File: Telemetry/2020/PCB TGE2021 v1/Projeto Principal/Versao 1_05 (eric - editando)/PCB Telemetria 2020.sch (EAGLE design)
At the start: 49 parts, among them IC1 INA240A1DR, IC2 MCP3221A6T-E_OTVAO, IC3 AZ1117IH-3.3TRG1, IC4 ACS758LCB-050B-PFF-T, IC5 ADS1115IDGSR, IC6 ACS712-030B3, IC7 THVD2410DR, J1 172042-0406

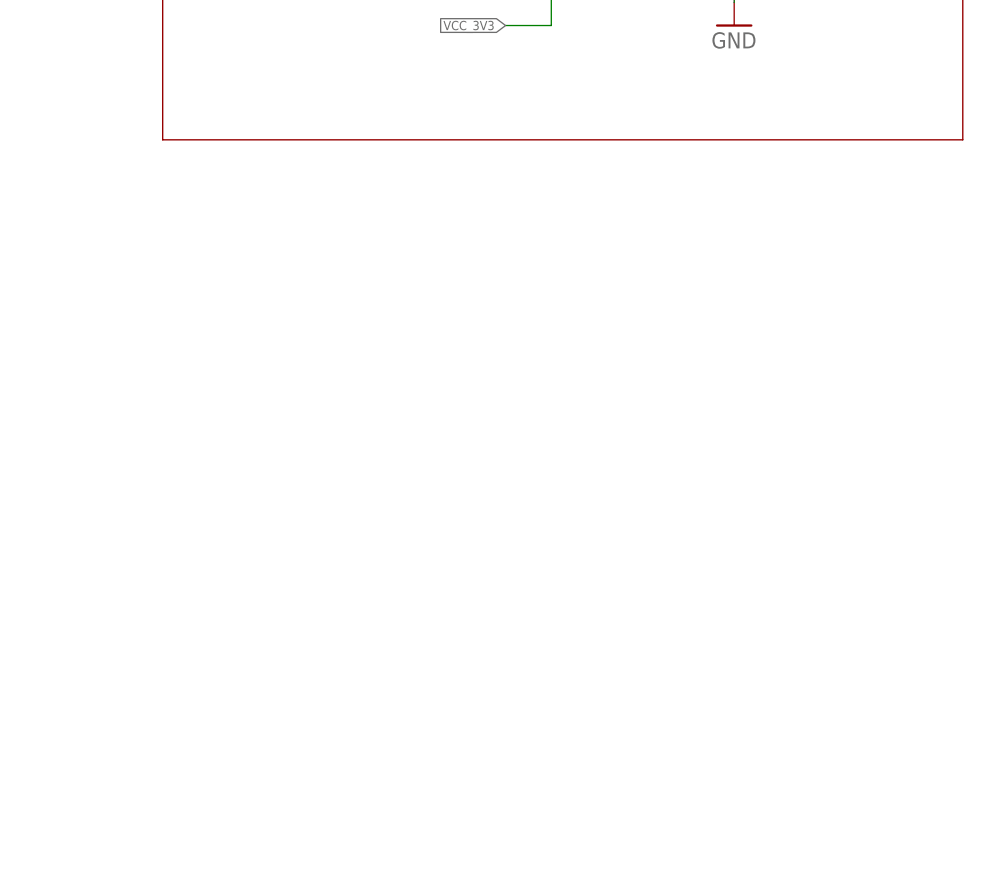
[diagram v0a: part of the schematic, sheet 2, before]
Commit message: Adding temperature sensor TMP100
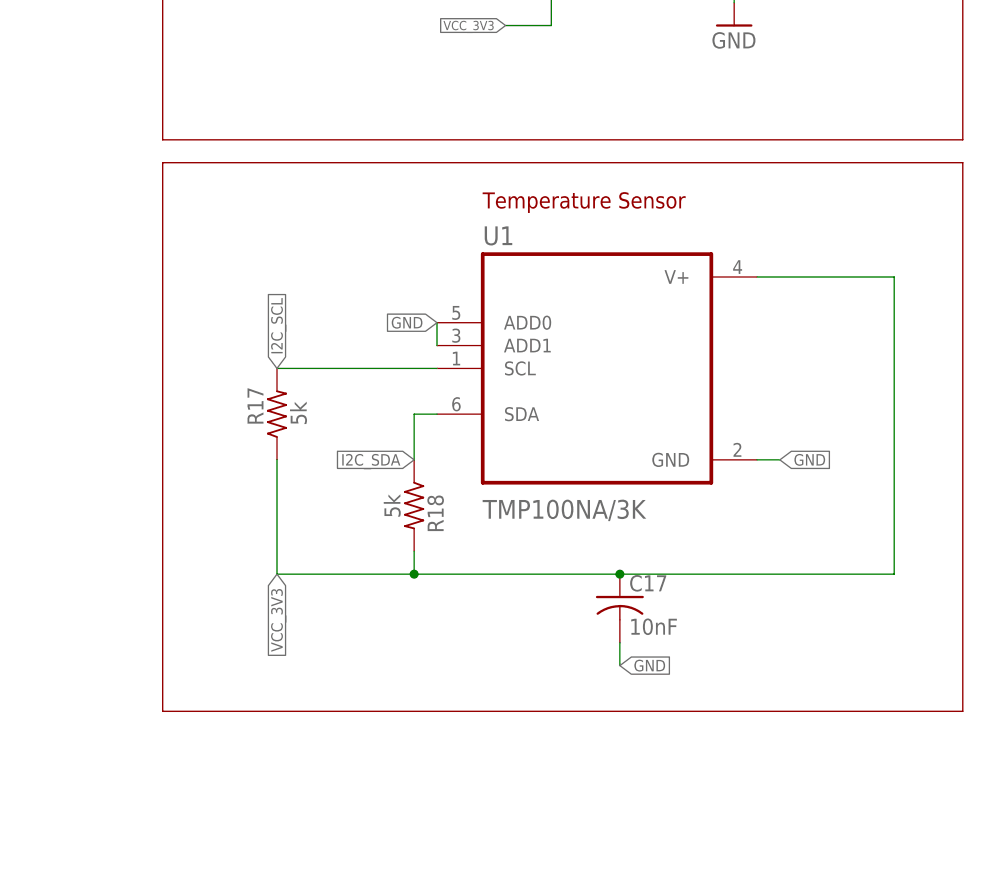
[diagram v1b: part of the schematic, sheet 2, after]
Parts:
- added C17: 10nF, rcl:C-USC0805
- added R17, R18: 5k, rcl:R-US_R0805
- added U1: TMP100NA/3K, TMP100NA_3K:TMP100NA/3K
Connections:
- net GND: now also C17.2, U1.ADD0, U1.ADD1, U1.GND
- net I2C_SCL: now also R17.2, U1.SCL
- net I2C_SDA: now also R18.1, U1.SDA
- net VCC_3V3: now also C17.1, R17.1, R18.2, U1.V+
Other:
- note added: "Temperature Sensor"
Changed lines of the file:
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@@
 <?xml version="1.0" encoding="utf-8"?>
 <!DOCTYPE eagle SYSTEM "eagle.dtd">
-<eagle version="9.5.2">
+<eagle version="9.6.2">
 <drawing>
 <settings>
@@
 <part name="SUPPLY5" library="supply2" library_urn="urn:adsk.eagle:library:372" deviceset="GND" device=""/>
 <part name="SUPPLY6" library="supply2" library_urn="urn:adsk.eagle:library:372" deviceset="GND" device=""/>
+<part name="U1" library="TMP100NA_3K" deviceset="TMP100NA/3K" device=""/>
+<part name="R17" library="rcl" library_urn="urn:adsk.eagle:library:334" deviceset="R-US_" device="R0805" package3d_urn="urn:adsk.eagle:package:23553/2" value="5k"/>
+<part name="R18" library="rcl" library_urn="urn:adsk.eagle:library:334" deviceset="R-US_" device="R0805" package3d_urn="urn:adsk.eagle:package:23553/2" value="5k"/>
+<part name="C17" library="rcl" library_urn="urn:adsk.eagle:library:334" deviceset="C-US" device="C0805" package3d_urn="urn:adsk.eagle:package:23617/2" value="10nF"/>
 </parts>
 <sheets>
@@
 <text x="365.76" y="194.564" size="1.778" layer="97" align="center">Output RC
 Filter</text>
+<wire x1="284.48" y1="142.24" x2="284.48" y2="81.28" width="0.1524" layer="94"/>
+<wire x1="284.48" y1="142.24" x2="373.38" y2="142.24" width="0.1524" layer="94"/>
+<wire x1="373.38" y1="81.28" x2="373.38" y2="142.24" width="0.1524" layer="94"/>
+<wire x1="284.48" y1="81.28" x2="373.38" y2="81.28" width="0.1524" layer="94"/>
+<text x="320.04" y="137.16" size="1.778" layer="94">Temperature Sensor</text>
 </plain>
 <instances>
@@
 <attribute name="NAME" x="326.1614" y="166.37" size="1.778" layer="95" rot="R90"/>
 <attribute name="VALUE" x="330.962" y="166.37" size="1.778" layer="96" rot="R90"/>
+</instance>
+<instance part="U1" gate="A" x="332.74" y="119.38" smashed="yes">
+<attribute name="NAME" x="320.04" y="133.08" size="2.0828" layer="95" ratio="10" rot="SR0"/>
+<attribute name="VALUE" x="320.04" y="102.68" size="2.0828" layer="96" ratio="10" rot="SR0"/>
+</instance>
+<instance part="R17" gate="G$1" x="297.18" y="114.3" smashed="yes" rot="R90">
+<attribute name="NAME" x="295.6814" y="113.03" size="1.778" layer="95" rot="R90"/>
+<attribute name="VALUE" x="300.482" y="113.03" size="1.778" layer="96" rot="R90"/>
+</instance>
+<instance part="R18" gate="G$1" x="312.42" y="104.14" smashed="yes" rot="R270">
+<attribute name="NAME" x="313.9186" y="105.41" size="1.778" layer="95" rot="R270"/>
+<attribute name="VALUE" x="309.118" y="105.41" size="1.778" layer="96" rot="R270"/>
+</instance>
+<instance part="C17" gate="G$1" x="335.28" y="93.98" smashed="yes">
+<attribute name="NAME" x="336.296" y="94.615" size="1.778" layer="95"/>
+<attribute name="VALUE" x="336.296" y="89.789" size="1.778" layer="96"/>
 </instance>
 </instances>
@@
 <wire x1="347.98" y1="160.02" x2="347.98" y2="162.56" width="0.1524" layer="91"/>
 </segment>
+<segment>
+<pinref part="U1" gate="A" pin="ADD0"/>
+<pinref part="U1" gate="A" pin="ADD1"/>
+<wire x1="314.96" y1="124.46" x2="314.96" y2="121.92" width="0.1524" layer="91"/>
+<label x="314.96" y="124.46" size="1.27" layer="95" rot="R180" xref="yes"/>
+</segment>
+<segment>
+<pinref part="U1" gate="A" pin="GND"/>
+<wire x1="350.52" y1="109.22" x2="353.06" y2="109.22" width="0.1524" layer="91"/>
+<label x="353.06" y="109.22" size="1.27" layer="95" xref="yes"/>
+</segment>
+<segment>
+<pinref part="C17" gate="G$1" pin="2"/>
+<wire x1="335.28" y1="88.9" x2="335.28" y2="86.36" width="0.1524" layer="91"/>
+<label x="335.28" y="86.36" size="1.27" layer="95" xref="yes"/>
+</segment>
 </net>
 <net name="VCC_3V3" class="0">
@@
 <wire x1="327.66" y1="157.48" x2="322.58" y2="157.48" width="0.1524" layer="91"/>
 </segment>
+<segment>
+<pinref part="R18" gate="G$1" pin="2"/>
+<pinref part="C17" gate="G$1" pin="1"/>
+<wire x1="312.42" y1="99.06" x2="312.42" y2="96.52" width="0.1524" layer="91"/>
+<wire x1="312.42" y1="96.52" x2="335.28" y2="96.52" width="0.1524" layer="91"/>
+<pinref part="R17" gate="G$1" pin="1"/>
+<wire x1="297.18" y1="109.22" x2="297.18" y2="96.52" width="0.1524" layer="91"/>
+<wire x1="297.18" y1="96.52" x2="312.42" y2="96.52" width="0.1524" layer="91"/>
+<junction x="312.42" y="96.52"/>
+<pinref part="U1" gate="A" pin="V+"/>
+<wire x1="350.52" y1="129.54" x2="365.76" y2="129.54" width="0.1524" layer="91"/>
+<wire x1="365.76" y1="129.54" x2="365.76" y2="96.52" width="0.1524" layer="91"/>
+<wire x1="365.76" y1="96.52" x2="335.28" y2="96.52" width="0.1524" layer="91"/>
+<junction x="335.28" y="96.52"/>
+<label x="297.18" y="96.52" size="1.27" layer="95" rot="R270" xref="yes"/>
+</segment>
 </net>
 <net name="MSHUNT_AMP" class="0">
@@
 <label x="76.2" y="200.66" size="1.27" layer="95" rot="R90" xref="yes"/>
 </segment>
+<segment>
+<pinref part="R18" gate="G$1" pin="1"/>
+<pinref part="U1" gate="A" pin="SDA"/>
+<wire x1="312.42" y1="109.22" x2="312.42" y2="114.3" width="0.1524" layer="91"/>
+<wire x1="312.42" y1="114.3" x2="314.96" y2="114.3" width="0.1524" layer="91"/>
+<label x="312.42" y="109.22" size="1.27" layer="95" rot="R180" xref="yes"/>
+</segment>
 </net>
 <net name="I2C_SCL" class="0">
@@
 <label x="73.66" y="200.66" size="1.27" layer="95" rot="R90" xref="yes"/>
 </segment>
-</net>
+<segment>
+<pinref part="R17" gate="G$1" pin="2"/>
+<pinref part="U1" gate="A" pin="SCL"/>
+<wire x1="297.18" y1="119.38" x2="314.96" y2="119.38" width="0.1524" layer="91"/>
+<label x="297.18" y="119.38" size="1.27" layer="95" rot="R90" xref="yes"/>
+</segment>
+</net>
